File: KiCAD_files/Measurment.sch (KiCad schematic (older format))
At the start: 69 parts, among them J1 Measurment_stage_outline_outp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, J2 Measurment_stage_outline_sign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, J3 Conn_01x02, U1 NMA1505SC, U2 AMC1100, U3 AMC1100, U4 AMC1311, U5 R-78C5.0-1.0, U6 AMS1117-3.3, U7 NMA1505SC

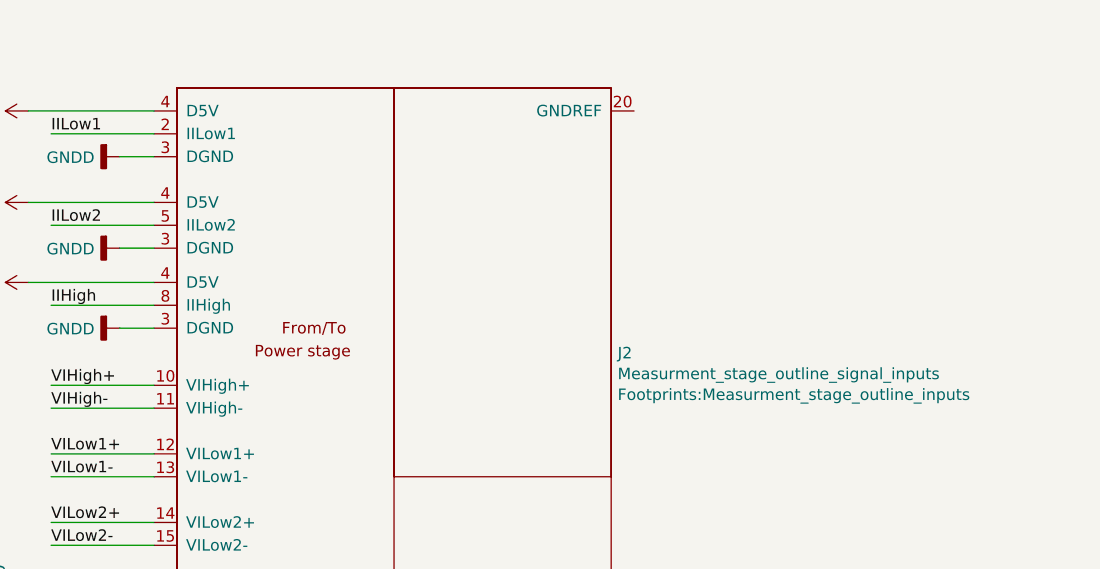
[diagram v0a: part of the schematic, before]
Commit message: Improved power board traces - Took a power electronic routing guideline into consideration.
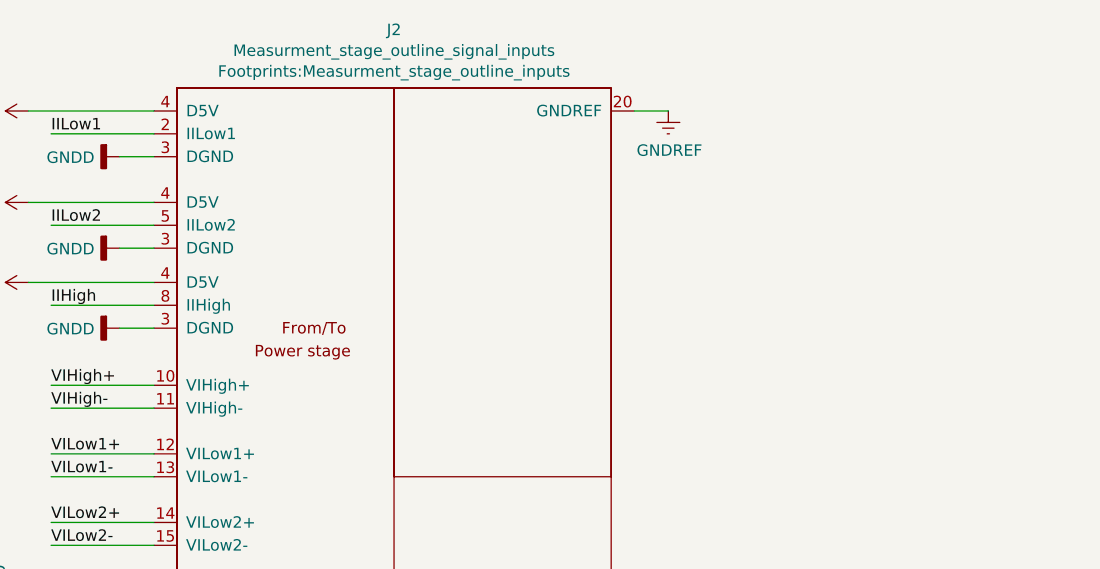
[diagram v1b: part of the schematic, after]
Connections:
- net GNDREF: now also J2.20 (GNDREF)
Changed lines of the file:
@@
 	12300 4000 12000 4000
-$Comp
-L Symbols:Measurment_stage_outline_signal_inputs J2
-U 1 1 606625D3
-P 13250 2050
-F 0 "J2" H 14278 2041 50  0000 L CNN
-F 1 "Measurment_stage_outline_signal_inputs" H 14278 1950 50  0000 L CNN
-F 2 "Footprints:Measurment_stage_outline_inputs" H 14278 1859 50  0000 L CNN
-F 3 "" H 12950 3450 50  0001 C CNN
-	1    13250 2050
-	1    0    0    -1
-$EndComp
-$Comp
-L Symbols:Measurment_stage_outline_outputs J1
-U 1 1 60677086
-P 13150 4300
-F 0 "J1" H 13200 4965 50  0000 C CNN
-F 1 "Measurment_stage_outline_outputs" H 13200 4874 50  0000 C CNN
-F 2 "Footprints:Measurment_stage_outline_outputs" H 12950 5050 50  0001 C CNN
-F 3 "" H 12950 5050 50  0001 C CNN
-	1    13150 4300
-	1    0    0    -1
-$EndComp
 $Comp
 L Connector_Generic:Conn_01x02 J3
@@
 Wire Wire Line
 	950  6100 1250 6100
+$Comp
+L Symbols:Measurment_stage_outline_signal_inputs J2
+U 1 1 5F4F5FF7
+P 13250 2050
+F 0 "J2" H 13300 3455 50  0000 C CNN
+F 1 "Measurment_stage_outline_signal_inputs" H 13300 3364 50  0000 C CNN
+F 2 "Footprints:Measurment_stage_outline_inputs" H 13300 3273 50  0000 C CNN
+F 3 "" H 12950 3450 50  0001 C CNN
+	1    13250 2050
+	1    0    0    -1
+$EndComp
+$Comp
+L Symbols:Measurment_stage_outline_outputs J1
+U 1 1 5F50BB94
+P 13150 4300
+F 0 "J1" H 13200 4965 50  0000 C CNN
+F 1 "Measurment_stage_outline_outputs" H 13200 4874 50  0000 C CNN
+F 2 "Footprints:Measurment_stage_outline_outputs" H 12950 5050 50  0001 C CNN
+F 3 "" H 12950 5050 50  0001 C CNN
+	1    13150 4300
+	1    0    0    -1
+$EndComp
+$Comp
+L power:GNDREF #PWR0144
+U 1 1 5F4A4B12
+P 14500 1000
+F 0 "#PWR0144" H 14500 750 50  0001 C CNN
+F 1 "GNDREF" H 14505 827 50  0000 C CNN
+F 2 "" H 14500 1000 50  0001 C CNN
+F 3 "" H 14500 1000 50  0001 C CNN
+	1    14500 1000
+	1    0    0    -1
+$EndComp
+Wire Wire Line
+	14500 1000 14350 1000
 $EndSCHEMATC

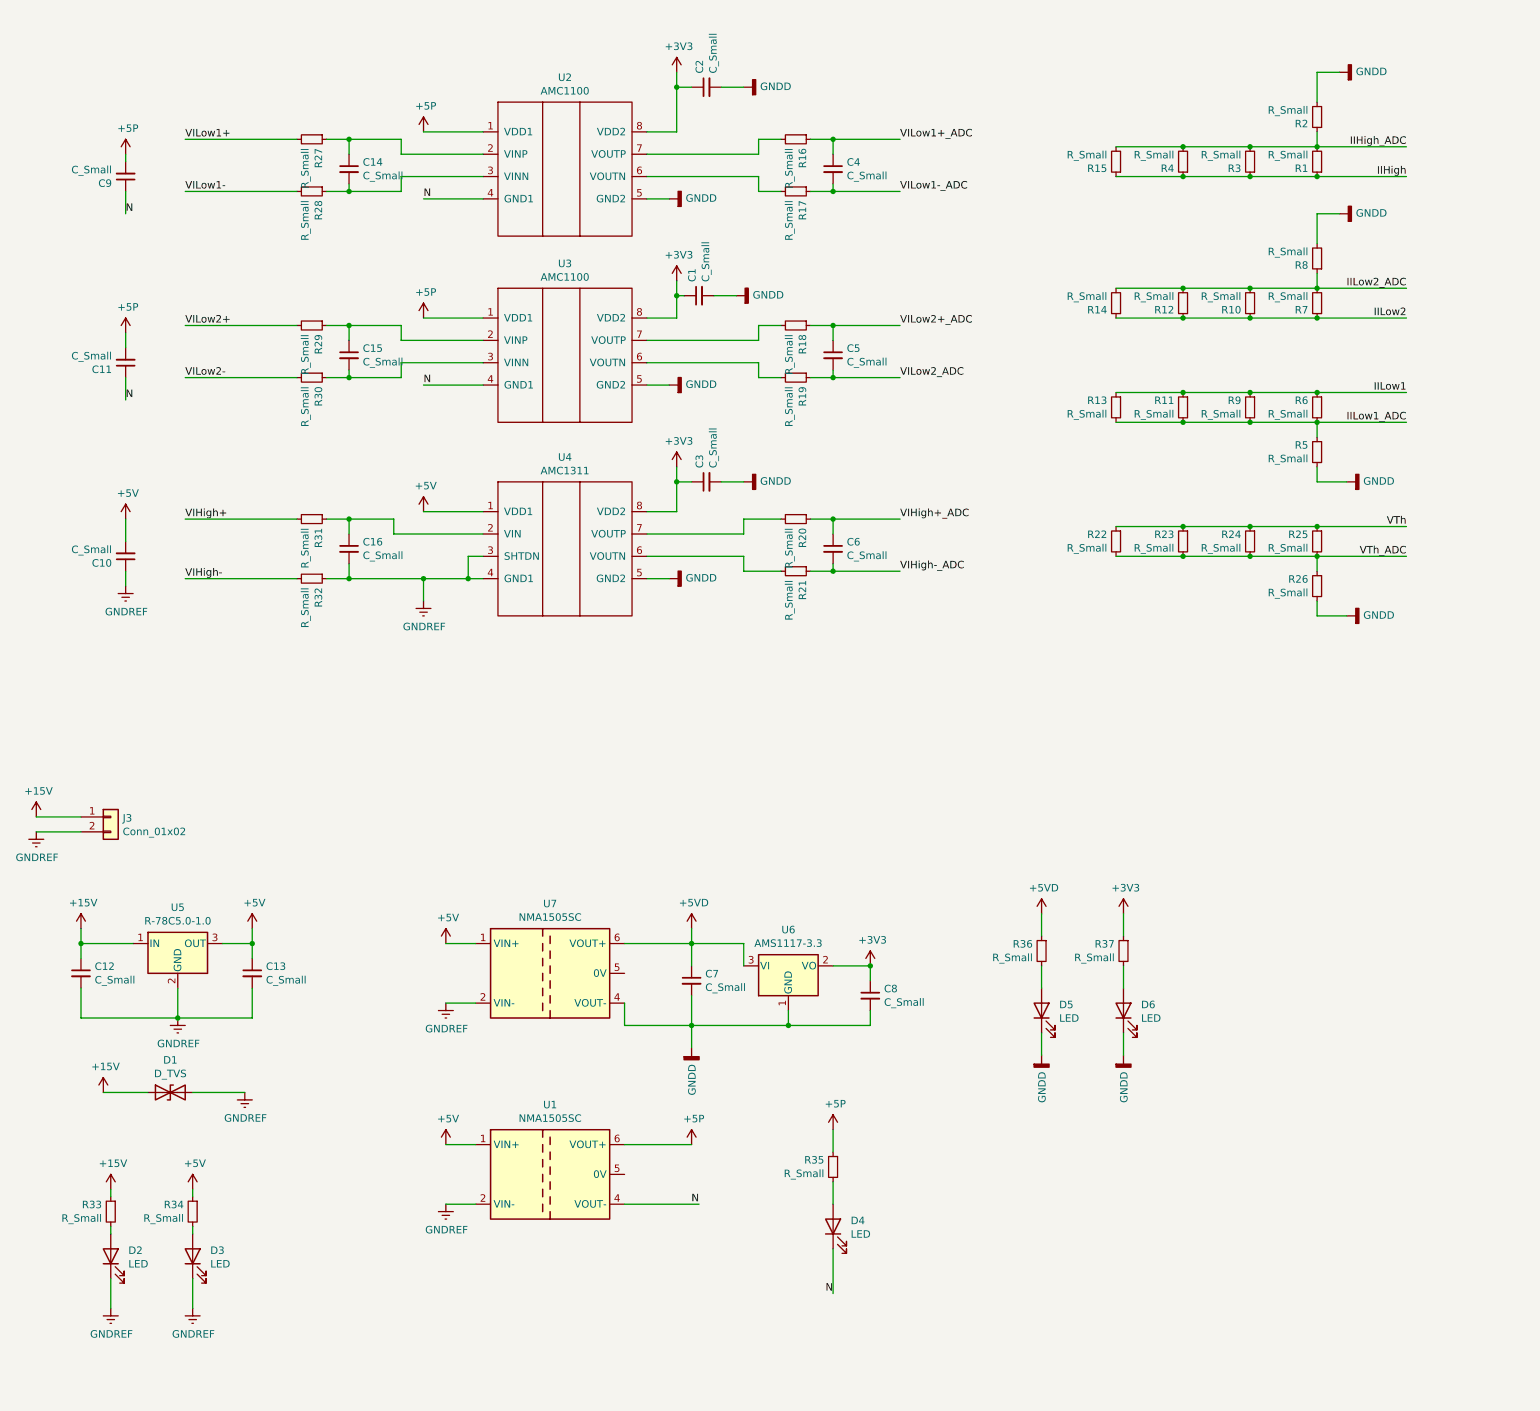
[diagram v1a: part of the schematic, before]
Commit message: Addded missing values and datasheet to measurment schematic Minor schematic modifications - added zener diodes
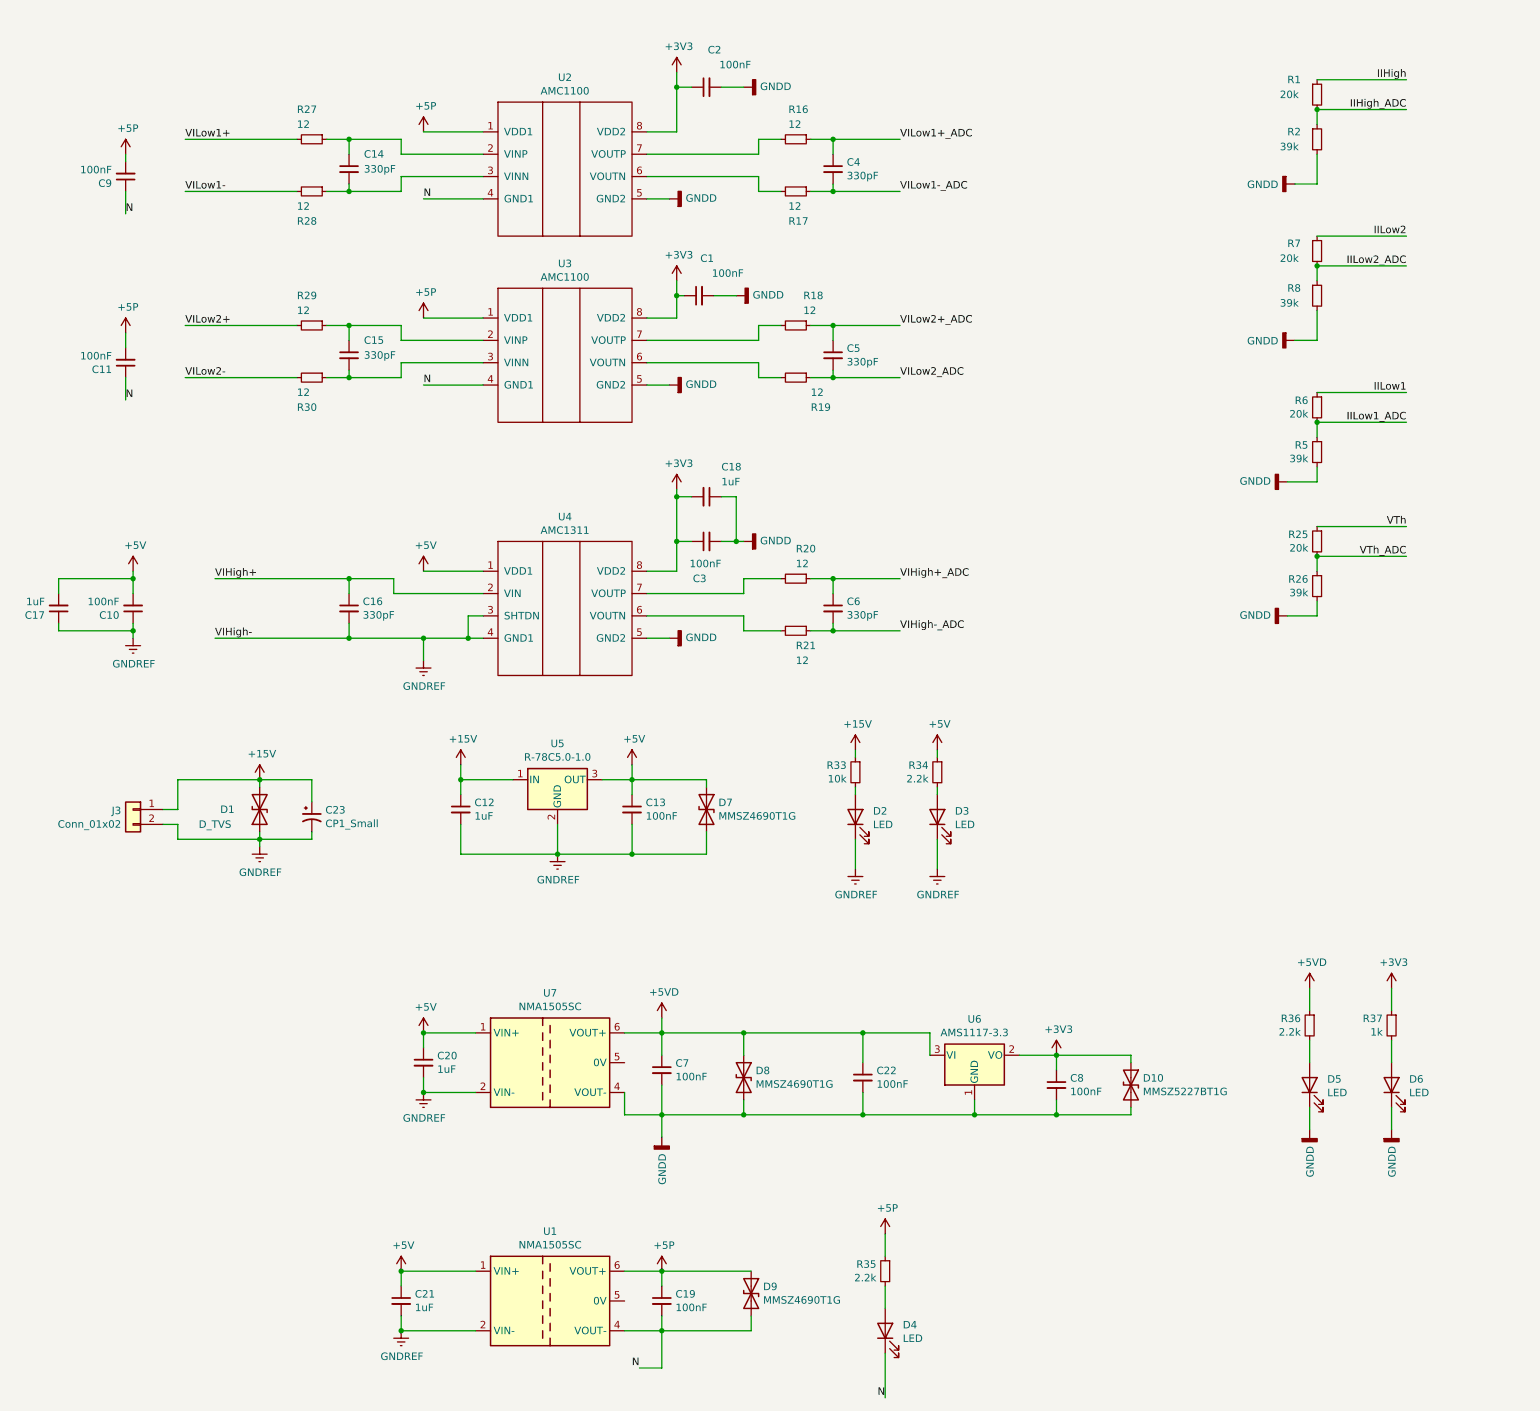
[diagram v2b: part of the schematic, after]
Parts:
- removed R10, R11, R12, R13, R14, R15, R22, R23, R24, R3, R31, R32, R4, R9: R_Small, Resistor_SMD:R_0805_2012Metric, symbol Device:R_Small
- added C17, C18, C20, C21: 1uF, Capacitor_SMD:C_0805_2012Metric, symbol Device:C_Small
- added C19, C22: 100nF, Capacitor_SMD:C_0805_2012Metric, symbol Device:C_Small
- added C23: CP1_Small, Capacitor_SMD:CP_Elec_5x5.9, symbol Device:CP1_Small
- added D10: MMSZ5227BT1G, Diode_SMD:D_SOD-123, symbol Device:D_TVS
- added D7, D8, D9: MMSZ4690T1G, Diode_SMD:D_SOD-123, symbol Device:D_TVS
- C1, C10, C11, C13, C2, C3, C7, C8, C9: value C_Small -> 100nF
- C12: value C_Small -> 1uF
- C14, C15, C16, C4, C5, C6: value C_Small -> 330pF
- R1, R25, R6, R7: value R_Small -> 20k
- R16, R17, R18, R19, R20, R21, R27, R28, R29, R30: value R_Small -> 12
- R2, R26, R5, R8: value R_Small -> 39k
- R33: value R_Small -> 10k
- R34, R35, R36: value R_Small -> 2.2k
- R37: value R_Small -> 1k
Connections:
- net VIHigh- is gone; now on net GNDREF: J2.11 (VIHigh-)
- net +15V: now also D1.2 (A2), C23.1; no longer D1.1 (A1)
- net +3V3: now also C18.2, D10.1 (A1)
- net +5P: now also C19.1, D9.1 (A1)
- net +5V: now also C17.2, C20.1, C21.1, D7.1 (A1)
- net +5VD: now also C22.1, D8.1 (A1)
- net GNDD: now also C18.1, C22.2, D10.2 (A2), D8.2 (A2)
- net GNDREF: now also D1.1 (A1), C17.1, C20.2, C21.2, C23.2, D7.2 (A2); no longer D1.2 (A2)
- net N: now also C19.2, D9.2 (A2)
- net VIHigh+: now also C16.1, U4.2 (VIN)
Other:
- moved on the sheet: C10, C12, C13, C16, C3, C6, C7, C8, D1, D2, D3, D4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

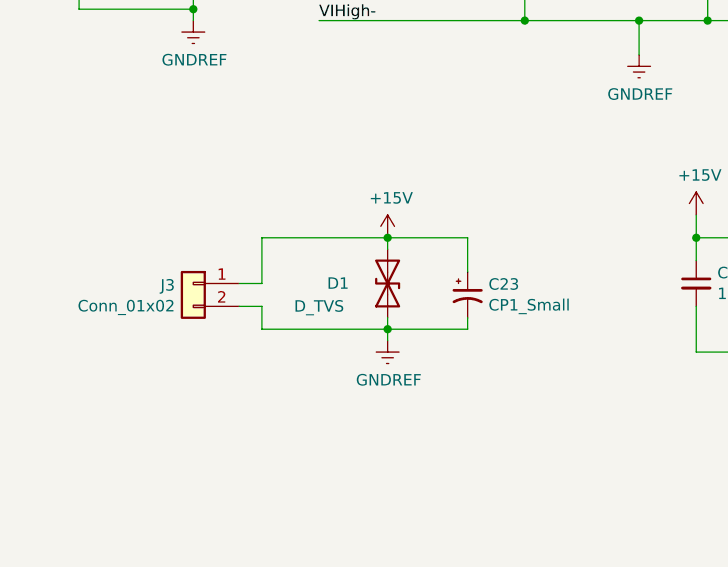
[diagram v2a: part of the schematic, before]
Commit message: Added BOM files
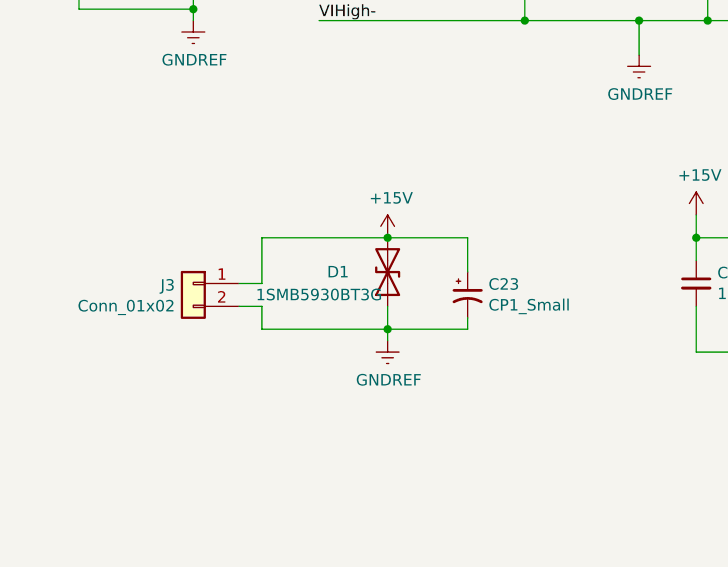
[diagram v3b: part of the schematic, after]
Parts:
- D1: value D_TVS -> 1SMB5930BT3G
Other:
- moved on the sheet: D1
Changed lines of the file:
@@
 L Device:D_TVS D1
 U 1 1 5F45D229
-P 2450 5950
-F 0 "D1" V 2450 6167 50  0000 C CNN
-F 1 "D_TVS" V 2350 6250 50  0000 C CNN
-F 2 "Diode_SMD:D_SMB" H 2450 5950 50  0001 C CNN
-F 3 "~" H 2450 5950 50  0001 C CNN
-	1    2450 5950
+P 2450 5900
+F 0 "D1" V 2450 6117 50  0000 C CNN
+F 1 "1SMB5930BT3G" V 2350 6200 50  0000 C CNN
+F 2 "Diode_SMD:D_SMB" H 2450 5900 50  0001 C CNN
+F 3 "https://www.onsemi.com/pub/Collateral/1SMB5913BT3-D.PDF" H 2450 5900 50  0001 C CNN
+	1    2450 5900
 	0    -1   -1   0
 $EndComp
@@
 Wire Wire Line
 	1900 5750 2450 5750
-Wire Wire Line
-	2450 5800 2450 5750
 Connection ~ 2450 5750
 Wire Wire Line
-	2450 6100 2450 6150
+	2450 6050 2450 6150
 Wire Wire Line
 	1900 6050 1900 6150

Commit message: Revision of the schematics - Part 1 of 3
The schematics of the measurement, driver and power parts were commented and reorganized.
Most of the work is focused on readeability. More detailed comments are to come.
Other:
- note added: "All inputs\ncome from \nthe power\nstage"
- note added: "All meas. signals\nare sent to the \nADC for sampling"
- note added: "Current adaptation chains"
- note added: "Gain = XXX / XXX = XXX"
- note added: "High-Voltage Bus"
- note added: "Input connector\nto power the board\nfrom an external\nvoltage source."
- note added: "Input voltage \n0 to 72V"
- note added: "Isolated 5V to 5V\nfeeder used to \npower the measurements\nreferenced to the digital \nground"
- note added: "Isolated 5V to 5V\nfeeder used to \npower the measurements\nrelative to the neutral"
- note added: "LEDs for verifying that all the parts of the feeder are\nopeartional"
- note added: "Measurement stage Inputs"
- note added: "Measurement stage Outputs"
- note added: "Non-Isolated 5V to 3.3V\nfeeder used to \npower the microcontroller\nand all its associated electronics"
- note added: "Non-isolated\n15V to 5V converter\nthat powers \nall the electronics\nof the converter"
- note added: "Power Channel 1"
- note added: "Power Channel 2"
- note added: "System Feeder"
- note added: "The 5V\nfeed and\nthe 15V \nfeed go to \nthe driver stage"
- note added: "The AMC1100 is an isolation op amp\nthat is used here with the low-side voltage \nmeasurement.\nThis components has input and ouptut\nfiltres which were implemented as per\nits datasheet. \nIt can measure AC voltage and DC voltage.\nIts AC measurement is centered around XXXXV."
- note added: "The AMC1311 is a high-precision isolation op amp\nthat is used here with the high-side voltage \nmeasurement.\nThis components has input and ouptut\nfiltres which were implemented as per\nits datasheet. \nIt can only measure DC voltage."
- note added: "This voltage divider was calculated \nas to convert XXX V in 0-5V range. \nIts resolution was calculated as follows:"
- note added: "Voltage measurement chains"
- moved on the sheet: C1, C10, C11, C12, C13, C14, C15, C16, C17, C18, C19, C2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
